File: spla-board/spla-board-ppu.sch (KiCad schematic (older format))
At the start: 15 parts, among them J5 Conn_02x04_Odd_Even, J6 Conn_02x02_Odd_Even, U10 SNES_PPU1, U11 SNES_PPU2, U12 VRAM, U13 VRAM

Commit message: schematic/pcb: First layout excersize; add footprints; tweak pin order on periphreal bus level shifters.
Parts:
- C10, C11, C12, C8, C9: footprint (none) -> Capacitor_SMD:C_0402_1005Metric
- J5: footprint (none) -> Connector_PinHeader_2.54mm:PinHeader_2x04_P2.54mm_Vertical
- J6: footprint (none) -> Connector_PinHeader_2.54mm:PinHeader_2x02_P2.54mm_Vertical
- R10, R11, R8, R9: footprint (none) -> Resistor_SMD:R_0402_1005Metric
- U10, U11: footprint (none) -> Package_QFP:PQFP-100_14x20mm_P0.65mm
- U12, U13: footprint (none) -> Package_SO:SSOP-28_5.3x10.2mm_P0.65mm
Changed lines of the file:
@@
 F 0 "U10" H 5650 9115 50  0000 C CNN
 F 1 "SNES_PPU1" H 5650 9024 50  0000 C CNN
-F 2 "" H 5700 8300 50  0001 C CNN
+F 2 "Package_QFP:PQFP-100_14x20mm_P0.65mm" H 5700 8300 50  0001 C CNN
 F 3 "" H 5700 8300 50  0001 C CNN
 	1    5650 6100
@@
 F 0 "U13" H 9050 4965 50  0000 C CNN
 F 1 "VRAM" H 9050 4874 50  0000 C CNN
-F 2 "" H 9050 4050 50  0001 C CNN
+F 2 "Package_SO:SSOP-28_5.3x10.2mm_P0.65mm" H 9050 4050 50  0001 C CNN
 F 3 "" H 9050 4050 50  0001 C CNN
 	1    9050 4050
@@
 F 0 "U12" H 9050 7265 50  0000 C CNN
 F 1 "VRAM" H 9050 7174 50  0000 C CNN
-F 2 "" H 9050 6350 50  0001 C CNN
+F 2 "Package_SO:SSOP-28_5.3x10.2mm_P0.65mm" H 9050 6350 50  0001 C CNN
 F 3 "" H 9050 6350 50  0001 C CNN
 	1    9050 6350
@@
 F 0 "R11" H 10520 5846 50  0000 L CNN
 F 1 "100" H 10520 5755 50  0000 L CNN
-F 2 "" V 10380 5800 50  0001 C CNN
+F 2 "Resistor_SMD:R_0402_1005Metric" V 10380 5800 50  0001 C CNN
 F 3 "~" H 10450 5800 50  0001 C CNN
 	1    10450 5800
@@
 F 0 "C11" H 10568 6146 50  0000 L CNN
 F 1 "56pF" H 10568 6055 50  0000 L CNN
-F 2 "" H 10488 5950 50  0001 C CNN
+F 2 "Capacitor_SMD:C_0402_1005Metric" H 10488 5950 50  0001 C CNN
 F 3 "~" H 10450 6100 50  0001 C CNN
 	1    10450 6100
@@
 F 0 "C8" H 6792 3146 50  0000 L CNN
 F 1 "0.1uF" H 6792 3055 50  0000 L CNN
-F 2 "" H 6700 3100 50  0001 C CNN
+F 2 "Capacitor_SMD:C_0402_1005Metric" H 6700 3100 50  0001 C CNN
 F 3 "~" H 6700 3100 50  0001 C CNN
 	1    6700 3100
@@
 F 0 "C12" H 13092 3146 50  0000 L CNN
 F 1 "0.1uF" H 13092 3055 50  0000 L CNN
-F 2 "" H 13000 3100 50  0001 C CNN
+F 2 "Capacitor_SMD:C_0402_1005Metric" H 13000 3100 50  0001 C CNN
 F 3 "~" H 13000 3100 50  0001 C CNN
 	1    13000 3100
@@
 F 0 "C9" H 9492 3246 50  0000 L CNN
 F 1 "0.1uF" H 9492 3155 50  0000 L CNN
-F 2 "" H 9400 3200 50  0001 C CNN
+F 2 "Capacitor_SMD:C_0402_1005Metric" H 9400 3200 50  0001 C CNN
 F 3 "~" H 9400 3200 50  0001 C CNN
 	1    9400 3200
@@
 F 0 "C10" H 9492 5546 50  0000 L CNN
 F 1 "0.1uF" H 9492 5455 50  0000 L CNN
-F 2 "" H 9400 5500 50  0001 C CNN
+F 2 "Capacitor_SMD:C_0402_1005Metric" H 9400 5500 50  0001 C CNN
 F 3 "~" H 9400 5500 50  0001 C CNN
 	1    9400 5500
@@
 F 0 "J5" H 7950 1867 50  0000 C CNN
 F 1 "Conn_02x04_Odd_Even" H 7950 1776 50  0000 C CNN
-F 2 "" H 7900 1550 50  0001 C CNN
+F 2 "Connector_PinHeader_2.54mm:PinHeader_2x04_P2.54mm_Vertical" H 7900 1550 50  0001 C CNN
 F 3 "~" H 7900 1550 50  0001 C CNN
 	1    7900 1550
@@
 F 0 "R10" H 8520 2146 50  0000 L CNN
 F 1 "10K" H 8520 2055 50  0000 L CNN
-F 2 "" V 8380 2100 50  0001 C CNN
+F 2 "Resistor_SMD:R_0402_1005Metric" V 8380 2100 50  0001 C CNN
 F 3 "~" H 8450 2100 50  0001 C CNN
 	1    8450 2100
@@
 F 0 "R9" H 7570 2146 50  0000 L CNN
 F 1 "10K" H 7570 2055 50  0000 L CNN
-F 2 "" V 7430 2100 50  0001 C CNN
+F 2 "Resistor_SMD:R_0402_1005Metric" V 7430 2100 50  0001 C CNN
 F 3 "~" H 7500 2100 50  0001 C CNN
 	1    7500 2100
@@
 F 0 "R8" H 7220 2146 50  0000 L CNN
 F 1 "10K" H 7220 2055 50  0000 L CNN
-F 2 "" V 7080 2100 50  0001 C CNN
+F 2 "Resistor_SMD:R_0402_1005Metric" V 7080 2100 50  0001 C CNN
 F 3 "~" H 7150 2100 50  0001 C CNN
 	1    7150 2100
@@
 F 0 "J6" H 13900 3867 50  0000 C CNN
 F 1 "Conn_02x02_Odd_Even" H 13900 3776 50  0000 C CNN
-F 2 "" H 13850 3650 50  0001 C CNN
+F 2 "Connector_PinHeader_2.54mm:PinHeader_2x02_P2.54mm_Vertical" H 13850 3650 50  0001 C CNN
 F 3 "~" H 13850 3650 50  0001 C CNN
 	1    13850 3650
@@
 F 0 "U11" H 12200 9115 50  0000 C CNN
 F 1 "SNES_PPU2" H 12200 9024 50  0000 C CNN
-F 2 "" H 12250 8300 50  0001 C CNN
+F 2 "Package_QFP:PQFP-100_14x20mm_P0.65mm" H 12250 8300 50  0001 C CNN
 F 3 "" H 12250 8300 50  0001 C CNN
 	1    12200 6100

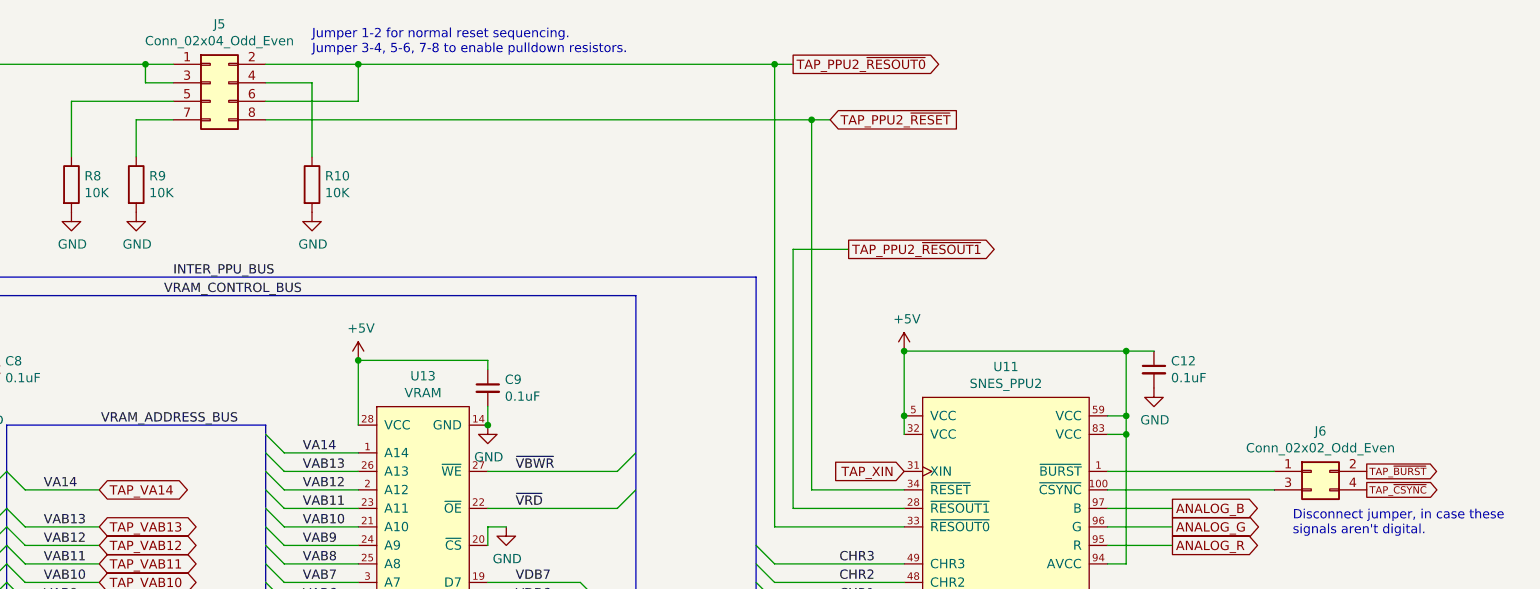
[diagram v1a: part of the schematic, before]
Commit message: schematic/pcb: Swap several footprints; rearrange pcb layout again.
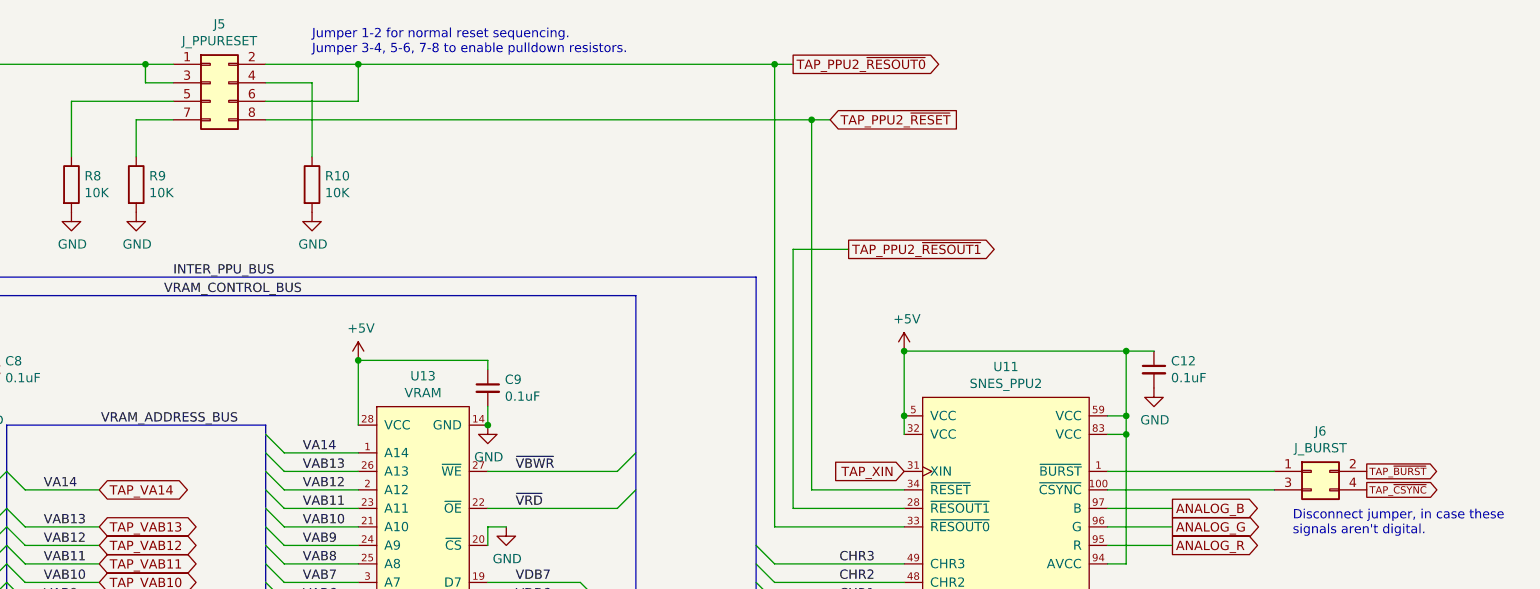
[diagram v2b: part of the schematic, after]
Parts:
- J5: value Conn_02x04_Odd_Even -> J_PPURESET
- J6: value Conn_02x02_Odd_Even -> J_BURST
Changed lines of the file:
@@
 P 7900 1550
 F 0 "J5" H 7950 1867 50  0000 C CNN
-F 1 "Conn_02x04_Odd_Even" H 7950 1776 50  0000 C CNN
+F 1 "J_PPURESET" H 7950 1776 50  0000 C CNN
 F 2 "Connector_PinHeader_2.54mm:PinHeader_2x04_P2.54mm_Vertical" H 7900 1550 50  0001 C CNN
 F 3 "~" H 7900 1550 50  0001 C CNN
@@
 P 13850 3650
 F 0 "J6" H 13900 3867 50  0000 C CNN
-F 1 "Conn_02x02_Odd_Even" H 13900 3776 50  0000 C CNN
+F 1 "J_BURST" H 13900 3776 50  0000 C CNN
 F 2 "Connector_PinHeader_2.54mm:PinHeader_2x02_P2.54mm_Vertical" H 13850 3650 50  0001 C CNN
 F 3 "~" H 13850 3650 50  0001 C CNN

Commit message: all: Correct spelling of 'peripheral'.
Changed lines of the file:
@@
 	10850 2600 4550 2600
 Text Label 8000 9500 0    50   ~ 0
-PERIPHREAL_BUS
+PERIPHERAL_BUS
 Wire Bus Line
 	4550 9500 11100 9500

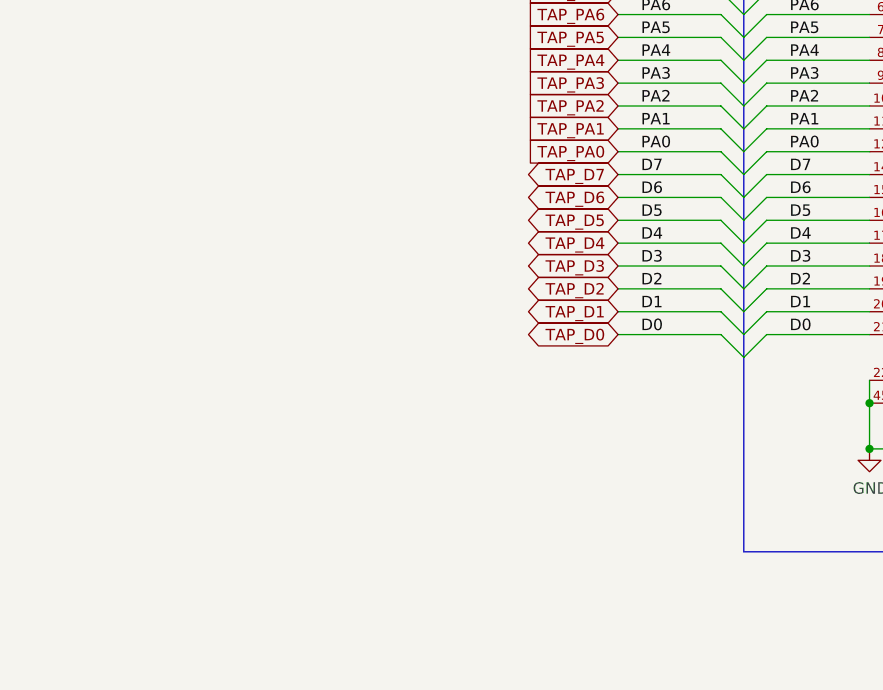
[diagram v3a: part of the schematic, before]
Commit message: schematic: Add pullup/pulldown jumper for peripheral data bus.
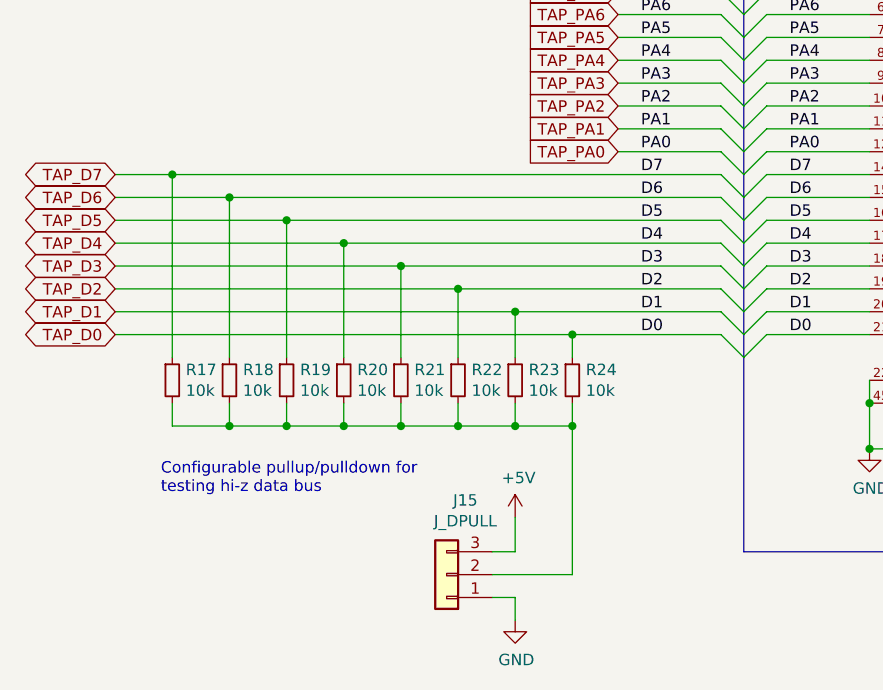
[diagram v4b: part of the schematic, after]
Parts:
- added J15: J_DPULL, symbol Connector_Generic:Conn_01x03
- added R17, R18, R19, R20, R21, R22, R23, R24: 10k, symbol Device:R_Small
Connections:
- net +5V: now also J15.3 (Pin_3)
- net GND: now also J15.1 (Pin_1)
- net TAP_D0: now also R24.1
- net TAP_D1: now also R23.1
- net TAP_D2: now also R22.1
- net TAP_D3: now also R21.1
- net TAP_D4: now also R20.1
- net TAP_D5: now also R19.1
- net TAP_D6: now also R18.1
- net TAP_D7: now also R17.1
- new net: J15.2 (Pin_2), R17.2, R18.2, R19.2, R20.2, R21.2, R22.2, R23.2, R24.2
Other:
- note added: "Configurable pullup/pulldown for\ntesting hi-z data bus"

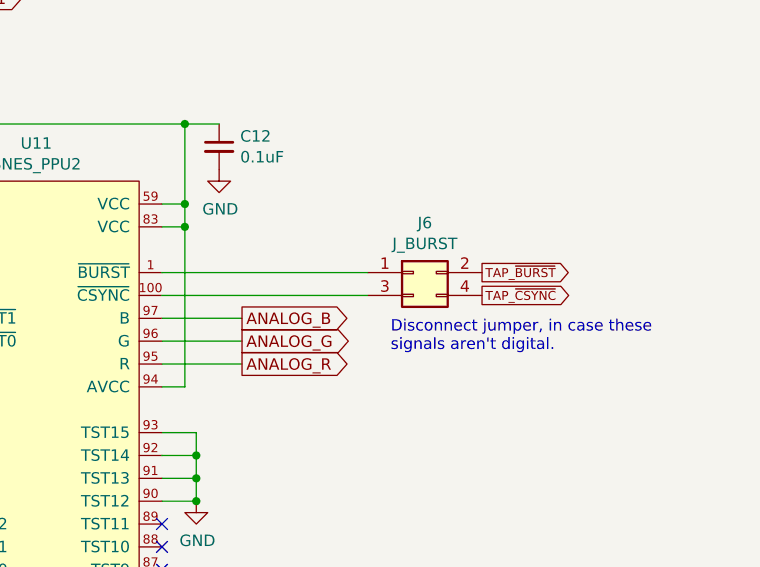
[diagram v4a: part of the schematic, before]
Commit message: schematic: Many minor tweaks.
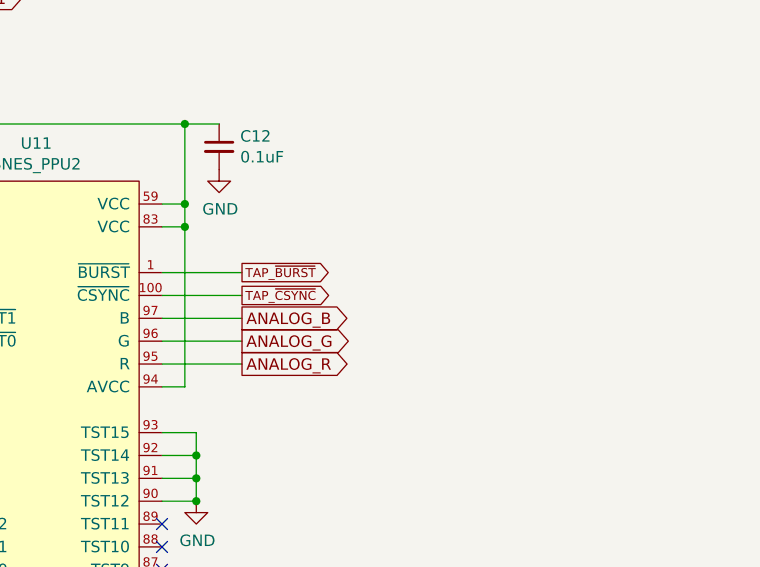
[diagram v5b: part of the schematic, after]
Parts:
- removed J6: J_BURST, Connector_PinHeader_2.54mm:PinHeader_2x02_P2.54mm_Vertical, symbol Connector_Generic:Conn_02x02_Odd_Even
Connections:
- net TAP_~BURST~: now also U11.1 (~BURST)
- net TAP_~CSYNC~: now also U11.100 (~CSYNC)
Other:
- note removed: "Disconnect jumper, in case these\nsignals aren't digital."
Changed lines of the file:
@@
 Wire Wire Line
 	11650 3000 12850 3000
-Text GLabel 14150 3650 2    39   Output ~ 0
+Text GLabel 13100 3650 2    39   Output ~ 0
 TAP_~BURST~
-Text GLabel 14150 3750 2    39   Output ~ 0
+Text GLabel 13100 3750 2    39   Output ~ 0
 TAP_~CSYNC~
 Text GLabel 13100 4050 2    50   Output ~ 0
@@
 	4650 1450 4550 1450
 Connection ~ 4650 1450
-$Comp
-L Connector_Generic:Conn_02x02_Odd_Even J6
-U 1 1 5F565BB7
-P 13850 3650
-F 0 "J6" H 13900 3867 50  0000 C CNN
-F 1 "J_BURST" H 13900 3776 50  0000 C CNN
-F 2 "Connector_PinHeader_2.54mm:PinHeader_2x02_P2.54mm_Vertical" H 13850 3650 50  0001 C CNN
-F 3 "~" H 13850 3650 50  0001 C CNN
-	1    13850 3650
-	1    0    0    -1
-$EndComp
-Wire Wire Line
-	12750 3650 13650 3650
-Wire Wire Line
-	12750 3750 13650 3750
-Text Notes 13750 4000 0    50   ~ 0
-Disconnect jumper, in case these\nsignals aren't digital.
+Wire Wire Line
+	12750 3650 13100 3650
+Wire Wire Line
+	12750 3750 13100 3750
 Text GLabel 5100 3650 0    50   Input ~ 0
 TAP_XIN
@@
 Wire Wire Line
 	3800 9600 3800 8950
+Connection ~ 3800 8950
+Text Notes 2000 9250 0    50   ~ 0
+Configurable pullup/pulldown for\ntesting hi-z data bus
 Wire Bus Line
 	10200 2700 10200 6050
@@
 Wire Bus Line
 	10000 4350 10000 9400
-Connection ~ 3800 8950
-Text Notes 2000 9250 0    50   ~ 0
-Configurable pullup/pulldown for\ntesting hi-z data bus
 $EndSCHEMATC
